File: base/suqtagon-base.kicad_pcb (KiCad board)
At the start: 2 copper layers, 100 x 86.6 mm, 31 parts, among them J1 USB_C_Receptacle_USB2.0, J2 Conn_01x04_Male, J3 Conn_01x04_Male, SW1 SW_Push, SW2 SW_Push, U1 AMS1117-3.3

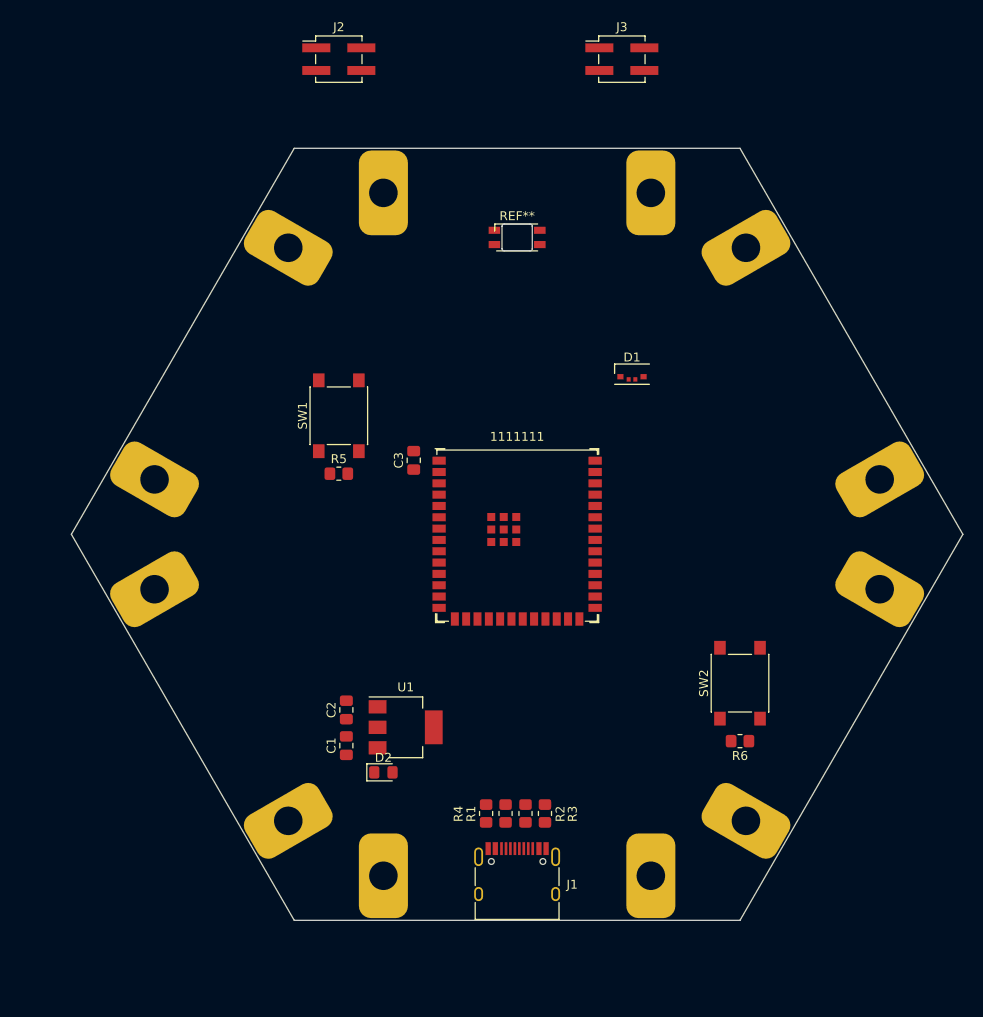
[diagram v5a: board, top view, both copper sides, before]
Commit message: added smd connectors footprint
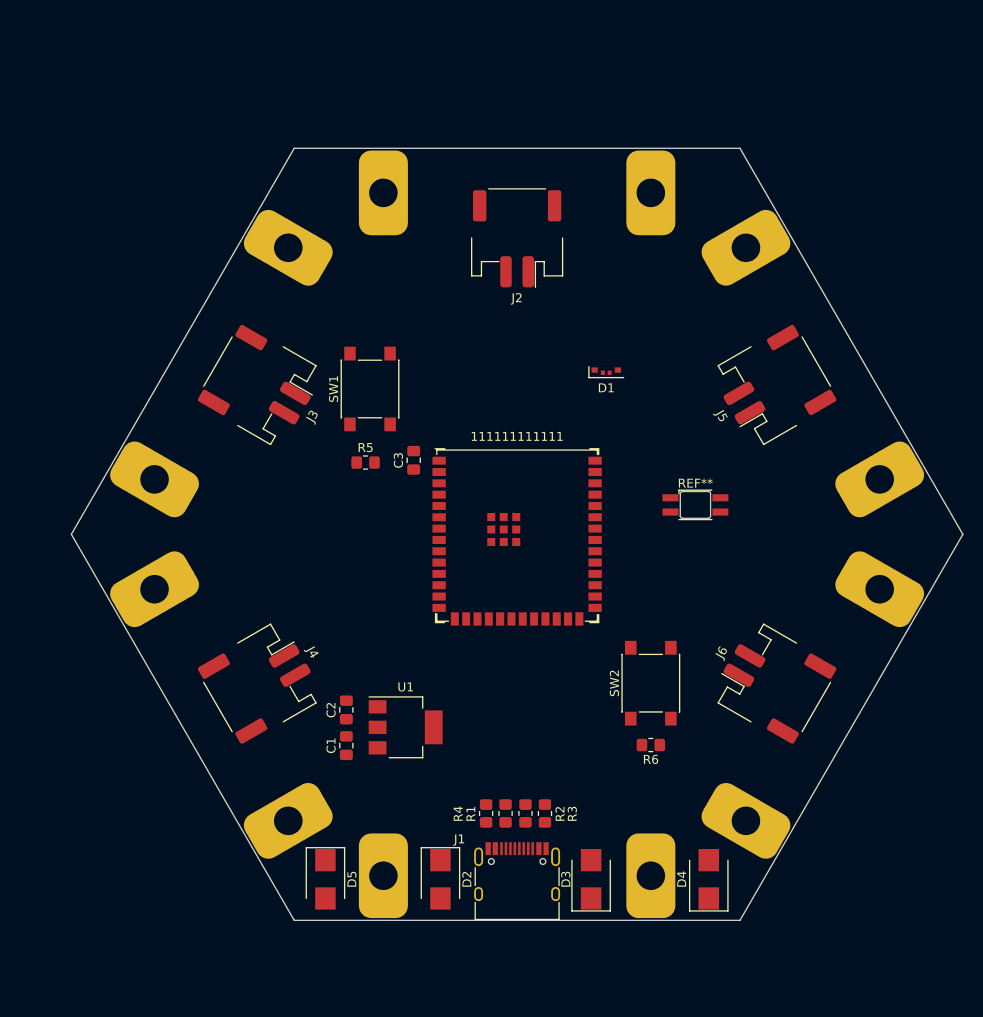
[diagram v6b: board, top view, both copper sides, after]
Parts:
- added D3: D_Schottky, Diode_SMD:D_SMB, F.Cu at (108.3, 132.0)
- added D4: D_Schottky, Diode_SMD:D_SMB, F.Cu at (121.5, 132.0)
- added D5: D_Schottky, Diode_SMD:D_SMB, F.Cu at (78.5, 132.0)
- added J4: Conn_01x02_Male, Connector_XH:XH _PH_2P_1x02_P2.54mm_Horizontal, F.Cu at (72.0, 109.5)
- added J5: Conn_01x02_Male, Connector_XH:XH _PH_2P_1x02_P2.54mm_Horizontal, F.Cu at (128.0, 77.2)
- added J6: Conn_01x02_Male, Connector_XH:XH _PH_2P_1x02_P2.54mm_Horizontal, F.Cu at (128.0, 109.5)
- D2: footprint Diode_SMD:D_0805_2012Metric_Pad1.15x1.40mm_HandSolder -> Diode_SMD:D_SMB
- J2, J3: value Conn_01x04_Male -> Conn_01x02_Male; footprint Connector_PinHeader_2.54mm:PinHeader_2x02_P2.54mm_Vertical_SMD -> Connector_XH:XH _PH_2P_1x02_P2.54mm_Horizontal
- moved J3 54.4 mm to (72.0, 77.2), turned to -120 degrees
- moved REF** 36.1 mm to (120.0, 90.0)
- moved J2 29.0 mm to (100.0, 61.0), turned to 180 degrees
- moved D2 13.6 mm to (91.4, 132.0), turned to -90 degrees
- moved R6 10.0 mm to (115.0, 116.9)
- moved SW2 10.0 mm to (115.0, 110.0)
- moved SW1 4.61 mm to (83.5, 77.0)
- moved R5 3.25 mm to (83.0, 85.2)
- moved D1 2.98 mm to (110.0, 75.0)
- renumbered 1111111 to 111111111111
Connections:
- C1 pad 1: Net-(C1-Pad1) -> VCC
- D2 pad 1: Net-(C1-Pad1) -> VCC
- D2 pad 2: VCC -> VBUS
- J1 pad A1: GND -> GNDA
- J1 pad A12: GND -> GNDA
- J1 pad A4: VCC -> VBUS
- J1 pad A9: VCC -> VBUS
- J1 pad B1: GND -> GNDA
- J1 pad B12: GND -> GNDA
- J1 pad B4: VCC -> VBUS
- J1 pad B9: VCC -> VBUS
- J2 pad 1: GND -> VBUS
- J2 pad 2: GND -> GNDA
- J3 pad 1: VCC -> VBUS
- J3 pad 2: VCC -> GNDA
- R3 pad 2: GND -> GNDA
- R4 pad 2: GND -> GNDA
- U1 pad 3: Net-(C1-Pad1) -> VCC

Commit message: started adding hand solder footprints
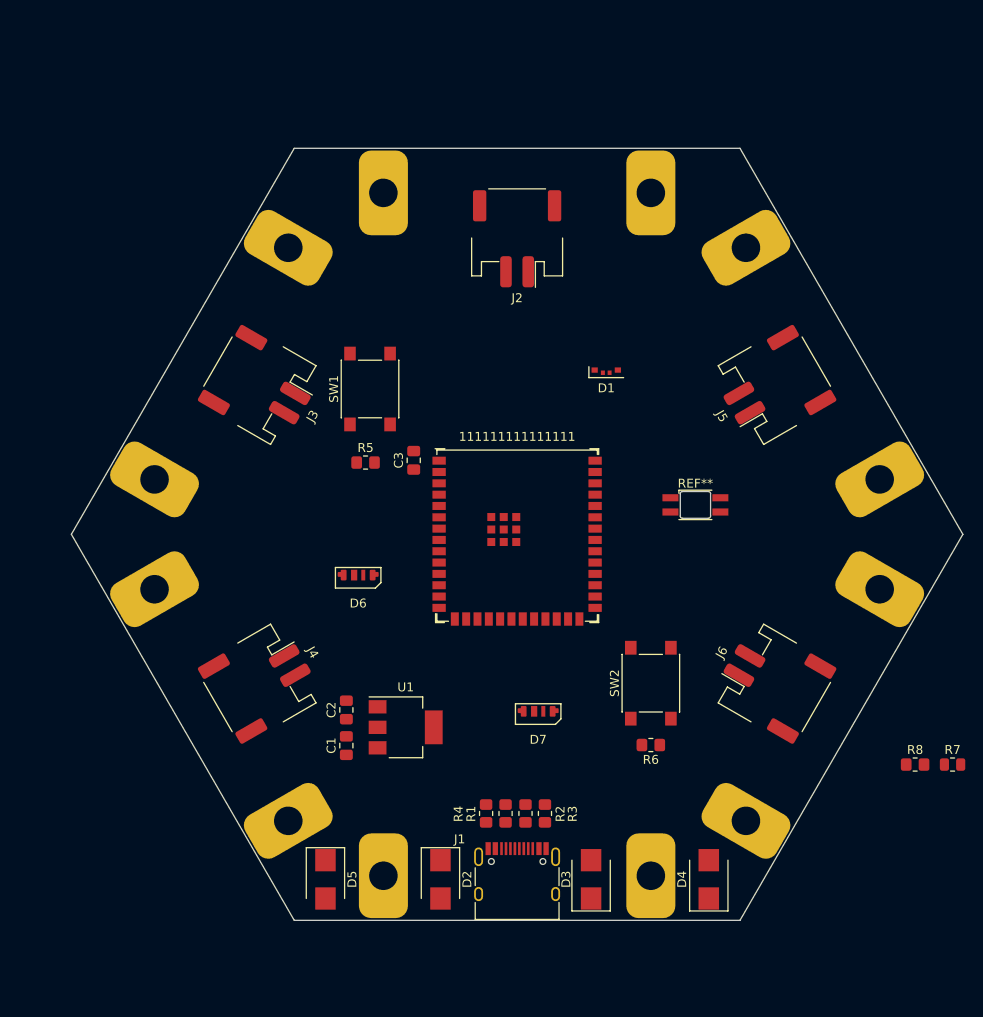
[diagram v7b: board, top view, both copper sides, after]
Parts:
- added D6: SK6812_SIDE_A, LED_SMD_SIDE:LED_SMD_SK6812_SIDE_A_4020, F.Cu at (82.2, 97.9)
- added D7: SK6812_SIDE_A, LED_SMD_SIDE:LED_SMD_SK6812_SIDE_A_4020, F.Cu at (102.4, 113.2)
- added R7: R, Resistor_SMD:R_0805_2012Metric, F.Cu at (148.8, 119.1)
- added R8: R, Resistor_SMD:R_0805_2012Metric_Pad1.20x1.40mm_HandSolder, F.Cu at (144.6, 119.1)
- renumbered 111111111111 to 111111111111111

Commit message: test background eb
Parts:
- removed R7: R, Resistor_SMD:R_0805_2012Metric
- removed R8: R, Resistor_SMD:R_0805_2012Metric_Pad1.20x1.40mm_HandSolder
- D6, D7: footprint LED_SMD_SIDE:LED_SMD_SK6812_SIDE_A_4020 -> LED_SMD_SIDE:LED_SMD_SK6812_SIDE_A_4020_HandSolder
- moved D6 7.71 mm to (80.7, 90.3)
- moved D7 2.43 mm to (102.6, 115.6)
